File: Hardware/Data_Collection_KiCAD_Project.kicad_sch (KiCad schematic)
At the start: 3 parts

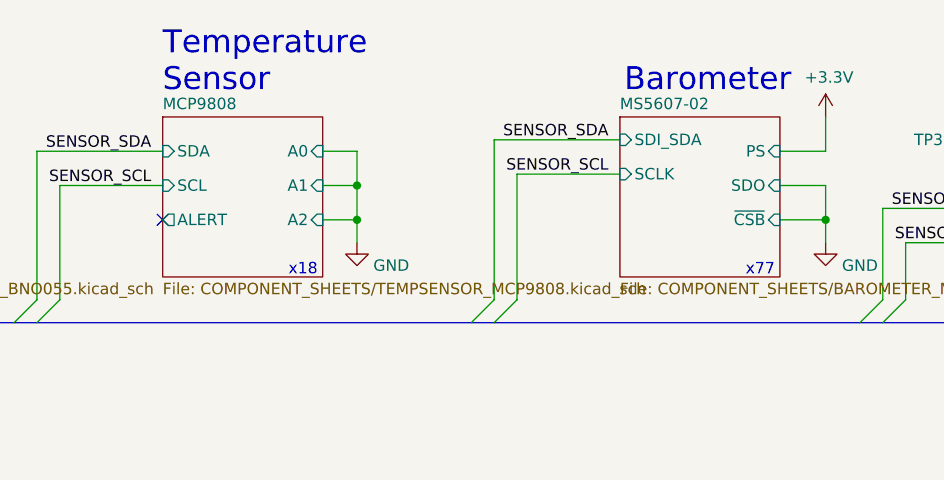
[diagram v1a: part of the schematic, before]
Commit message: Replaced Temp Sense and finalized routing
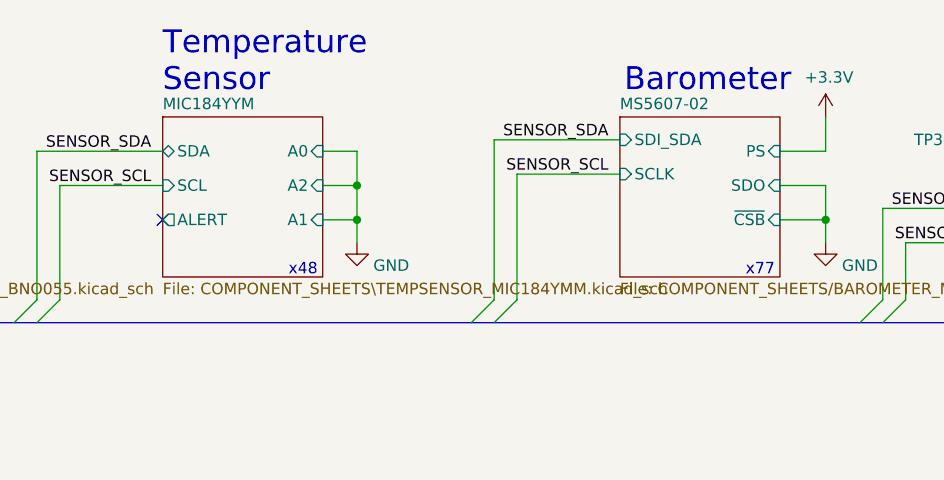
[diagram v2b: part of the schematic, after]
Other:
- removed sheet MCP9808
- added sheet MIC184YYM (COMPONENT_SHEETS\TEMPSENSOR_MIC184YMM.kicad_sch)
- note added: "x48"
- note removed: "x18"
